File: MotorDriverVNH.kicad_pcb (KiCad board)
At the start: 2 copper layers, 16.5 x 13.7 mm, 4 parts, among them IC1 VNH7070ASTR, J1 Conn_01x02, J3 Conn_01x05

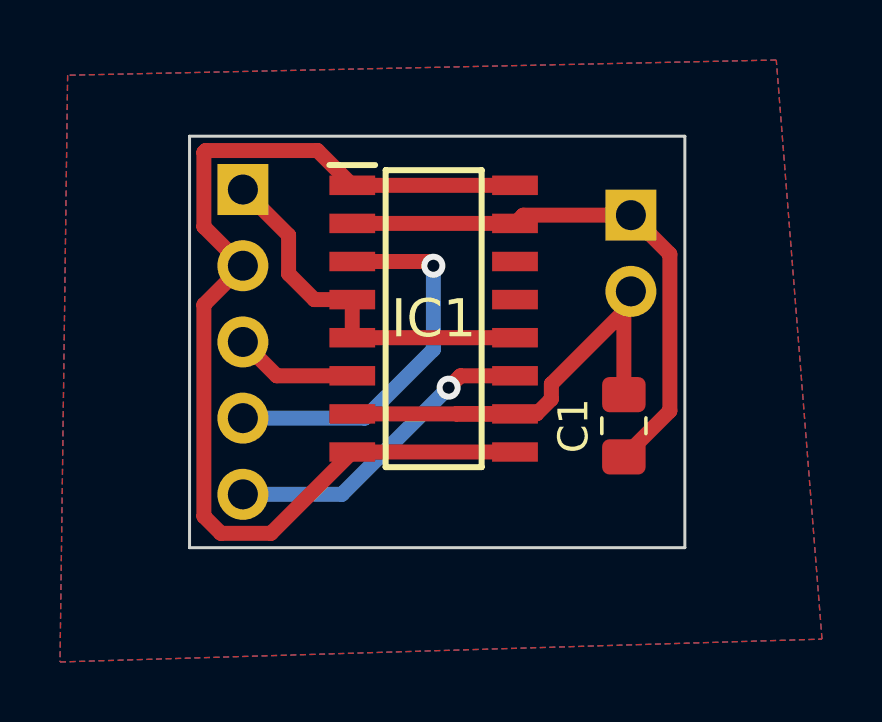
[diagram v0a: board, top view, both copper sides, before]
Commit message: Added Resistors
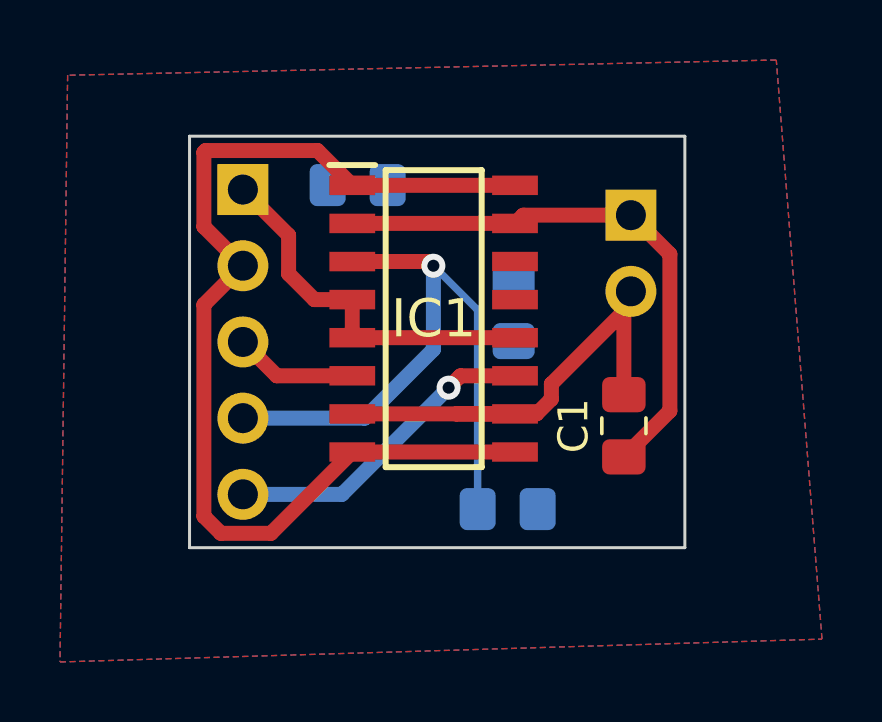
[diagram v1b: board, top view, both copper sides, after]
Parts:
- added R1: 100, Resistor_SMD:R_0805_2012Metric_Pad1.20x1.40mm_HandSolder, B.Cu at (80.2, 77.2)
- added R2: 100, Resistor_SMD:R_0805_2012Metric_Pad1.20x1.40mm_HandSolder, B.Cu at (75.2, 66.4)
- added R3: 100, Resistor_SMD:R_0805_2012Metric_Pad1.20x1.40mm_HandSolder, B.Cu at (80.4, 70.6)
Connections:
- IC1 pad 11: PWM -> Net-(IC1-PWM)
- IC1 pad 3: Direction1 -> Net-(IC1-IN_A)
- IC1 pad 6: Direction2 -> Net-(IC1-IN_B)
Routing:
- net Direction1: track 12.9 -> 21.6 mm

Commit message: Routed Resistors
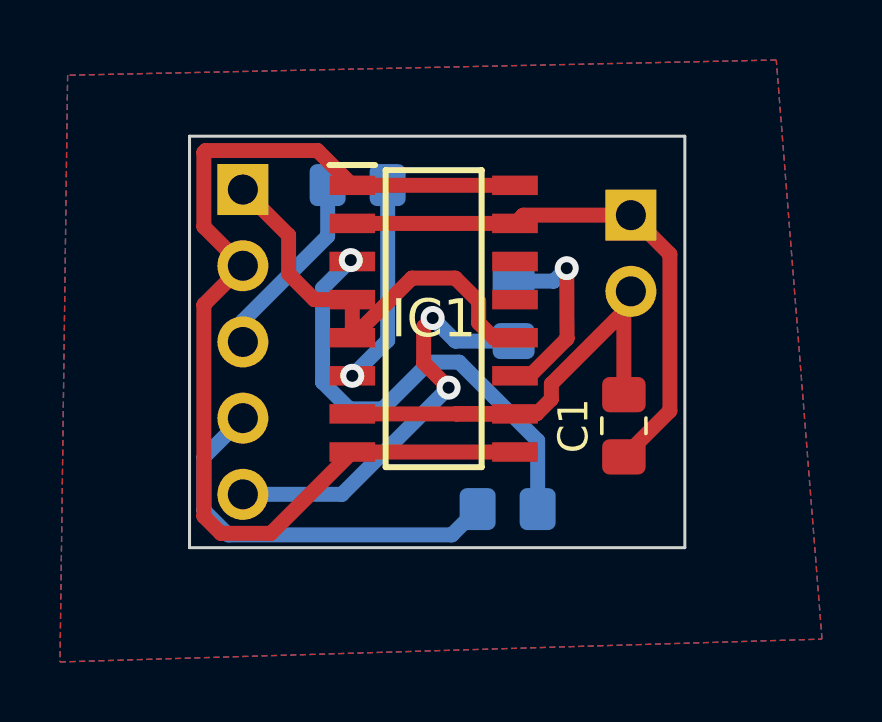
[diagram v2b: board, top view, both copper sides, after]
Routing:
- net Net-(IC1-IN_A): track 0.00 -> 16.0 mm, vias 0 -> 1
- net Direction1: track 21.6 -> 13.4 mm, vias 1 -> 0
- net Net-(IC1-IN_B): track 0.00 -> 6.85 mm, vias 0 -> 1
- net Net-(IC1-PWM): track 0.00 -> 6.58 mm, vias 0 -> 1
- net PWM: track 10.7 -> 14.2 mm, vias 1 -> 2
- net Direction2: track 4.11 -> 6.40 mm
- net 12v: track 12.6 -> 14.7 mm
